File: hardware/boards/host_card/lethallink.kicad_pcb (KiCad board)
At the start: 6 copper layers, 121.2 x 98.4 mm, 218 parts, among them J1 PCIe-x4, J2 USB3_Micro_B_Amphenol, J3 Conn_02x05_Odd_Even, J4 Conn_02x04_Odd_Even, J5 Conn_02x04_Odd_Even, J6 SODIMM_260, Q1 Q_NMOS_GSD, Q2 Q_NMOS_GSD, Q3 Q_NMOS_GSD, Q4 Q_NMOS_GSD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

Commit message: Some more messing about with the DDR3 modules
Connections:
- U8 pad N2: Net-(U8-PadN2) -> /DDR3 Cache/A3
- U8 pad N3: Net-(U8-PadN3) -> /DDR3 Cache/A0
- U8 pad P2: Net-(U8-PadP2) -> /DDR3 Cache/A5
- U8 pad P3: Net-(U8-PadP3) -> /DDR3 Cache/A2
- U8 pad P7: Net-(U8-PadP7) -> /DDR3 Cache/A1
- U8 pad P8: Net-(U8-PadP8) -> /DDR3 Cache/A4
- U8 pad R2: Net-(U8-PadR2) -> /DDR3 Cache/A7
- U8 pad R3: Net-(U8-PadR3) -> /DDR3 Cache/A9
- U8 pad R8: Net-(U8-PadR8) -> /DDR3 Cache/A6
- U8 pad T8: Net-(U8-PadT8) -> /DDR3 Cache/A8

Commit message: Roughly grouped unplaced parts together based on what they are related to
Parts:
- added D12: RClamp0512, lethalbit:RClamp0512, F.Cu at (25.8, 57.5)
- moved D10 230.4 mm to (36.2, 167.0)
- moved C54 227.6 mm to (30.8, 167.1)
- moved R51 223.9 mm to (26.8, 166.9)
- moved R47 223.6 mm to (43.0, 162.4)
- moved R49 223.0 mm to (26.8, 162.9)
- moved R50 221.7 mm to (26.8, 158.2)
- moved D9 220.9 mm to (35.9, 162.9)
- moved Q6 219.6 mm to (36.1, 158.2)
- moved R48 218.7 mm to (31.0, 163.2)
- moved SW2 213.2 mm to (27.2, 150.4)
- moved C27 212.2 mm to (103.9, 175.2)
- moved D8 211.5 mm to (31.4, 158.1)
- moved C23 207.3 mm to (103.2, 173.4)
- moved C24 207.3 mm to (95.2, 169.4)
- moved C26 207.3 mm to (101.2, 175.4)
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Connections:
- net Net-(U4-PadB7) renamed /DDR3 Cache/DQSU0-
- net Net-(U4-PadC7) renamed /DDR3 Cache/DQSU0+
- net Net-(U4-PadD3) renamed /DDR3 Cache/DMU0
- net Net-(U4-PadE7) renamed /DDR3 Cache/DML0
- net Net-(U4-PadF3) renamed /DDR3 Cache/DQSL0+
- net Net-(U4-PadG3) renamed /DDR3 Cache/DQSL0-
- net Net-(U8-PadB7) renamed /DDR3 Cache/DQSU1-
- net Net-(U8-PadC7) renamed /DDR3 Cache/DQSU1+
- net Net-(U8-PadD3) renamed /DDR3 Cache/DMU1
- net Net-(U8-PadE7) renamed /DDR3 Cache/DML1
- net Net-(U8-PadF3) renamed /DDR3 Cache/DQSL1+
- net Net-(U8-PadG3) renamed /DDR3 Cache/DQSL1-
- U4 pad J3: Net-(U4-PadJ3) -> /DDR3 Cache/~RAS
- U4 pad J7: Net-(U4-PadJ7) -> /DDR3 Cache/CK+
- U4 pad K1: Net-(U4-PadK1) -> /DDR3 Cache/ODT
- U4 pad K3: Net-(U4-PadK3) -> /DDR3 Cache/~CAS
- U4 pad K7: Net-(U4-PadK7) -> /DDR3 Cache/CK-
- U4 pad K9: Net-(U4-PadK9) -> /DDR3 Cache/CKE
- U4 pad L2: Net-(U4-PadL2) -> /DDR3 Cache/~CS
- U4 pad L3: Net-(U4-PadL3) -> /DDR3 Cache/~WE
- U4 pad T2: Net-(U4-PadT2) -> /DDR3 Cache/~RESET
- U8 pad J3: Net-(U8-PadJ3) -> /DDR3 Cache/~RAS
- U8 pad J7: Net-(U8-PadJ7) -> /DDR3 Cache/CK+
- U8 pad K1: Net-(U8-PadK1) -> /DDR3 Cache/ODT
- U8 pad K3: Net-(U8-PadK3) -> /DDR3 Cache/~CAS
- U8 pad K7: Net-(U8-PadK7) -> /DDR3 Cache/CK-
- U8 pad K9: Net-(U8-PadK9) -> /DDR3 Cache/CKE
- U8 pad L2: Net-(U8-PadL2) -> /DDR3 Cache/~CS
- U8 pad L3: Net-(U8-PadL3) -> /DDR3 Cache/~WE
- U8 pad T2: Net-(U8-PadT2) -> /DDR3 Cache/~RESET
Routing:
- net GND: track 63.8 -> 64.1 mm, vias 72 -> 73

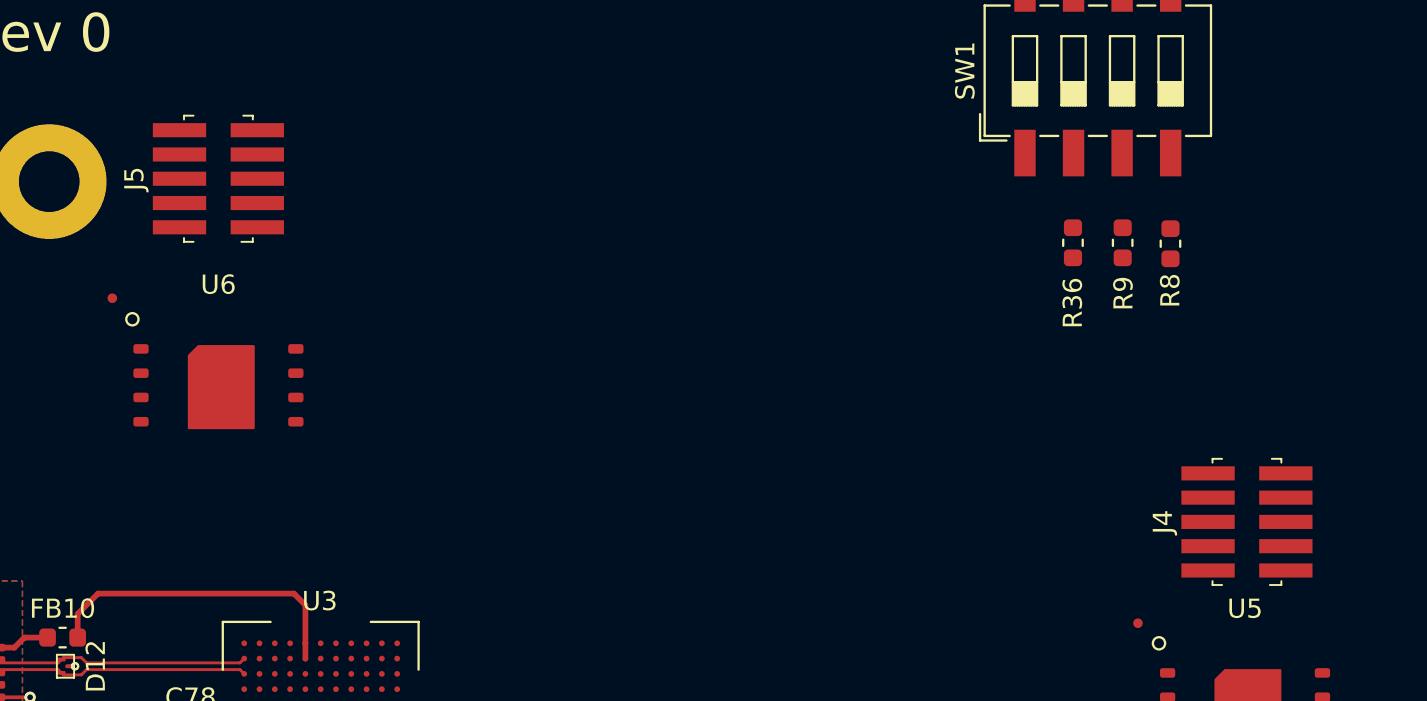
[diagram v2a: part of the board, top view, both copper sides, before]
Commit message: Added a pin-header for the FPGA SPI flash lines to allow for the USB PHY to do a DFU update of the gateware when closed
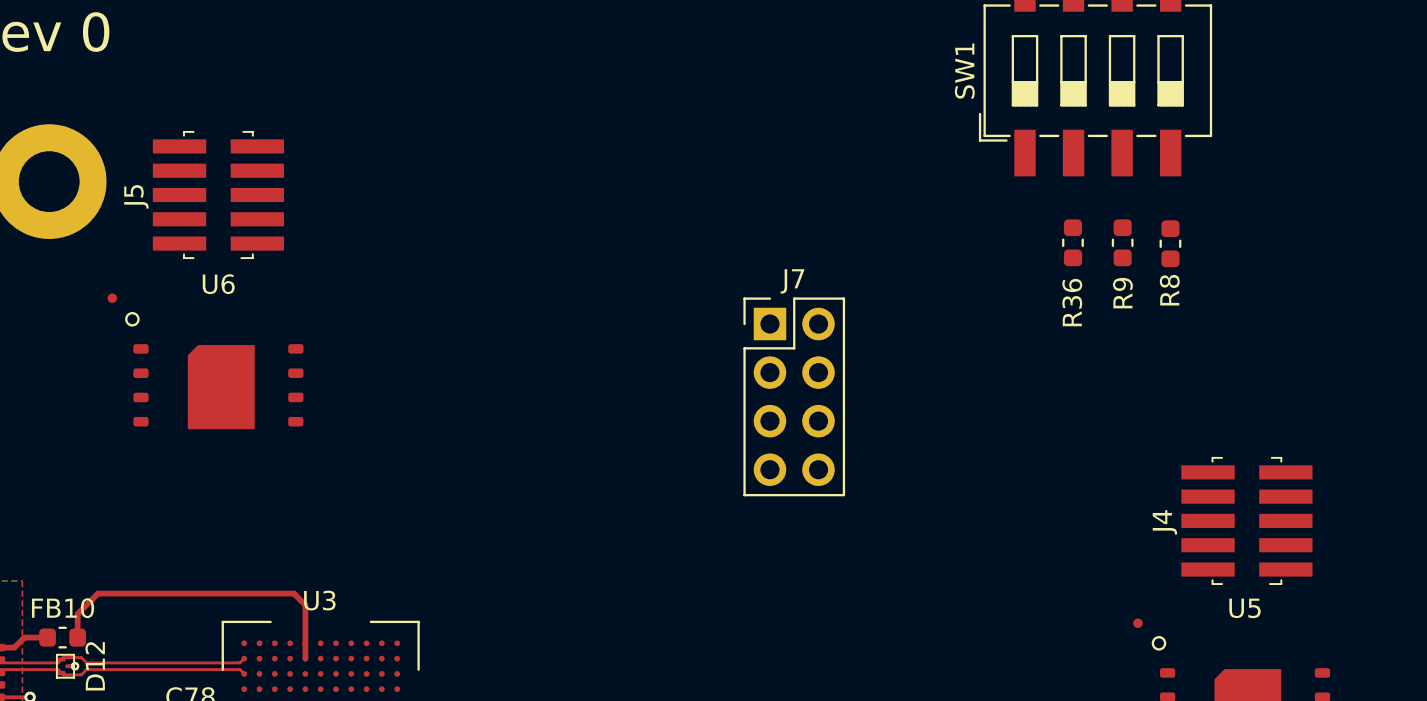
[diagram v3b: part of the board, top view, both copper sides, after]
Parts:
- added J7: Conn_02x04_Odd_Even, Connector_PinHeader_2.54mm:PinHeader_2x04_P2.54mm_Vertical, F.Cu at (62.6, 39.5)
- moved J5 0.85 mm to (33.8, 32.8)
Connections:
- J4 pad 1: /Boot Config/~RESET -> /Boot Config/~INIT
- J4 pad 2: /Boot Config/~INIT -> /Boot Config/~RESET
- J4 pad 3: +3V3 -> GND
- J4 pad 4: GND -> +3V3
- J5 pad 1: /Boot Config/~PHY_RESET -> GND
- J5 pad 2: GND -> /Boot Config/~PHY_RESET
- J5 pad 3: +3V3 -> GND
- J5 pad 4: GND -> +3V3
- J5 pad 5: Net-(J5-Pad5) -> /Boot Config/FPGA_DI
- J5 pad 7: Net-(J5-Pad7) -> /Boot Config/FPGA_CLK
- J5 pad 8: Net-(J5-Pad8) -> /Boot Config/FPGA_DO
- R42 pad 1: Net-(J4-Pad8) -> Net-(J4-Pad7)
- R43 pad 2: Net-(J4-Pad5) -> Net-(J4-Pad6)
- R44 pad 2: Net-(J4-Pad7) -> Net-(J4-Pad8)
- R45 pad 2: Net-(J4-Pad10) -> Net-(J4-Pad9)
- R46 pad 2: Net-(J4-Pad6) -> Net-(J4-Pad5)
- U1 pad R2: Net-(J4-Pad9) -> Net-(J4-Pad10)
- U1 pad V2: Net-(J4-Pad6) -> Net-(J4-Pad5)
- U1 pad W1: Net-(J4-Pad10) -> Net-(J4-Pad9)
- U1 pad W2: Net-(J4-Pad7) -> Net-(J4-Pad8)
- U1 pad Y2: Net-(J4-Pad5) -> Net-(J4-Pad6)
- U3 pad C1: Net-(J5-Pad9) -> Net-(J5-Pad10)
- U3 pad C2: Net-(J5-Pad7) -> /Boot Config/FPGA_DO
- U3 pad C4: Net-(U3-PadC4) -> /Boot Config/~FPGA_CS
- U3 pad D4: Net-(J5-Pad8) -> /Boot Config/FPGA_CLK
- U3 pad D5: Net-(J5-Pad6) -> /Boot Config/FPGA_DI
- U5 pad 1: Net-(J4-Pad9) -> Net-(J4-Pad10)
- U5 pad 2: Net-(J4-Pad7) -> Net-(J4-Pad8)
- U5 pad 3: Net-(J4-Pad5) -> Net-(J4-Pad6)
- U5 pad 5: Net-(J4-Pad6) -> Net-(J4-Pad5)
- U5 pad 6: Net-(J4-Pad8) -> Net-(J4-Pad7)
- U5 pad 7: Net-(J4-Pad10) -> Net-(J4-Pad9)
- U6 pad 1: Net-(J5-Pad9) -> Net-(J5-Pad10)
- U6 pad 2: Net-(J5-Pad7) -> /Boot Config/FPGA_DO
- U6 pad 3: Net-(J5-Pad5) -> Net-(J5-Pad6)
- U6 pad 5: Net-(J5-Pad6) -> /Boot Config/FPGA_DI
- U6 pad 6: Net-(J5-Pad8) -> /Boot Config/FPGA_CLK
- U6 pad 7: Net-(J5-Pad10) -> Net-(J5-Pad9)

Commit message: Hooked up the PCIe SMBUS and JTAG lines to the FPGA, might need to shuffle the signals around a little bit to get it to route nicely
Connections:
- U1 pad J4: Net-(U1-PadJ4) -> /AUX Control/PCIe_TMS
- U1 pad K4: Net-(U1-PadK4) -> /AUX Control/PCIe_TDO
- U1 pad L1: Net-(U1-PadL1) -> /AUX Control/PCIe_SMCLK
- U1 pad M1: Net-(U1-PadM1) -> /AUX Control/PCIe_SMDAT
- U1 pad M4: Net-(U1-PadM4) -> /AUX Control/PCIe_TCK
- U1 pad N4: Net-(U1-PadN4) -> /AUX Control/PCIe_TDI
- U1 pad P4: Net-(U1-PadP4) -> /AUX Control/PCIe_TRST#

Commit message: Added the remainder of the PCIe aux signals to the FPGA
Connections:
- U1 pad P1: Net-(U1-PadP1) -> /AUX Control/CLKREQ#
- U1 pad P2: Net-(U1-PadP2) -> /AUX Control/WAKE#
- U1 pad P3: Net-(U1-PadP3) -> /AUX Control/PERST#

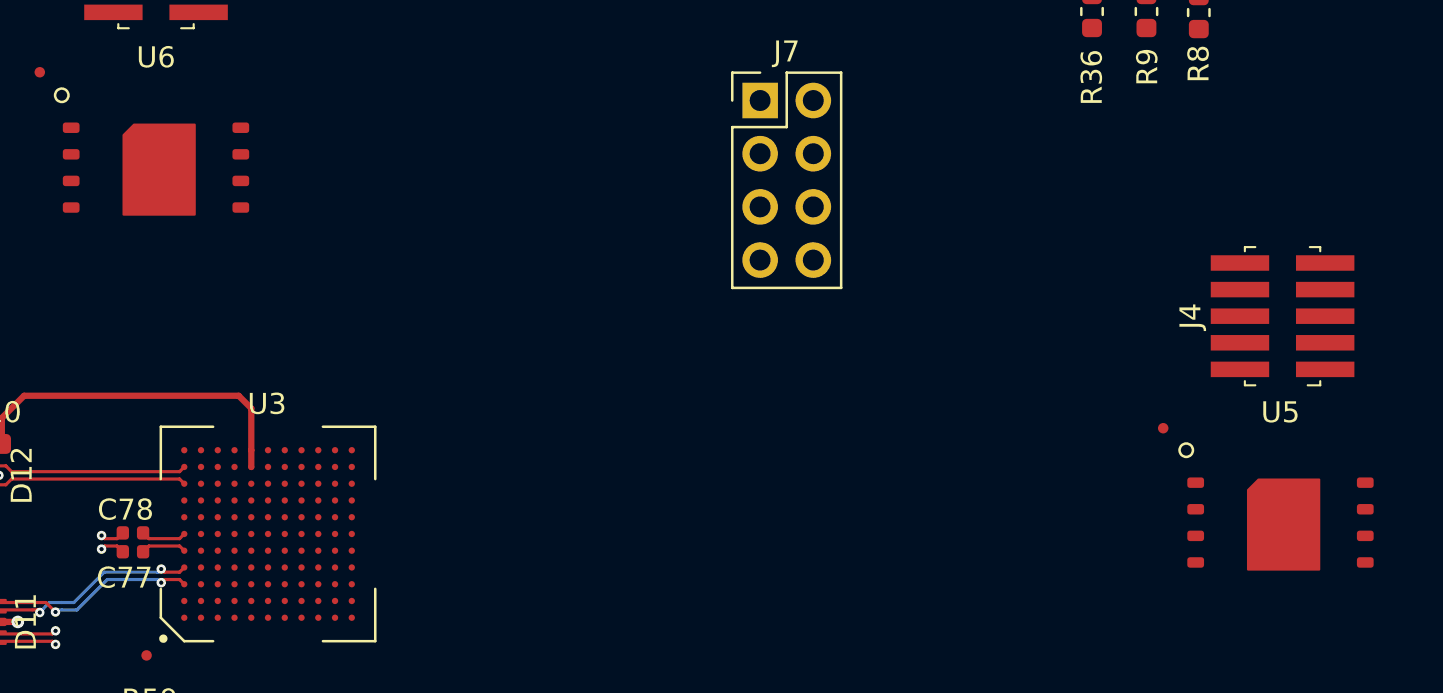
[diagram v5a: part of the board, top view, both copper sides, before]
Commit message: Updated the SPI flash footprints to have the exposed pad joined to the gnd properly
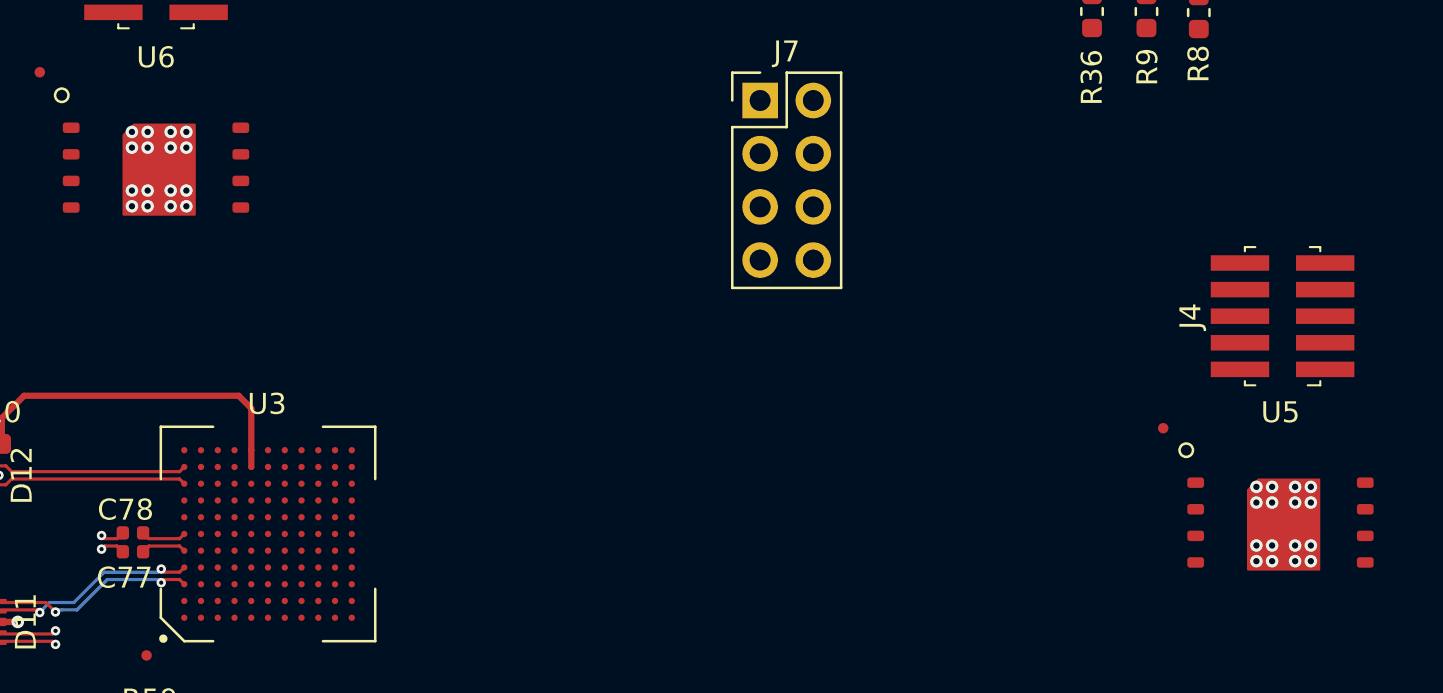
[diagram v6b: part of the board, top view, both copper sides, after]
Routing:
- net GND: vias 73 -> 105

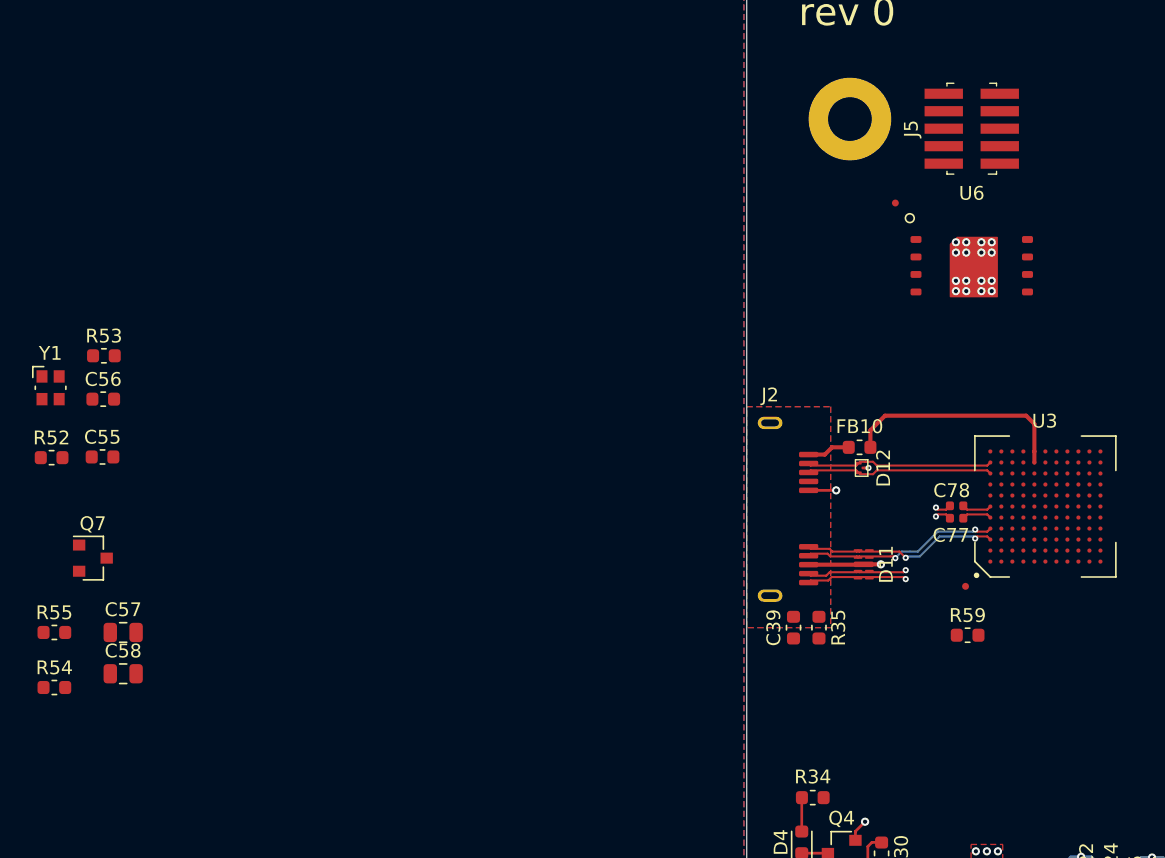
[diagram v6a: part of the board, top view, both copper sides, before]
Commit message: Started poking the SPI flash for the USB PHY
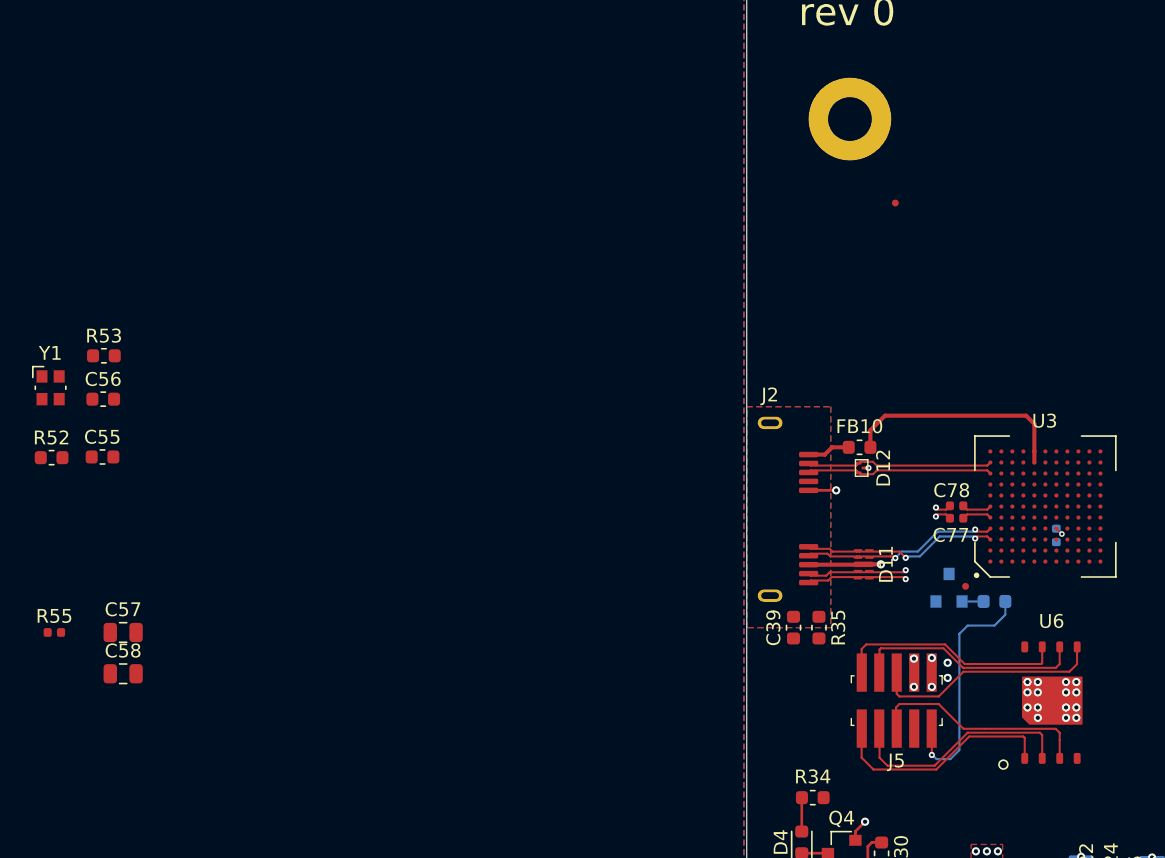
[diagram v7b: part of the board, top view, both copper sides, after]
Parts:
- Q7, R54: moved to B.Cu
- R55: footprint Resistor_SMD:R_0603_1608Metric -> Resistor_SMD:R_0402_1005Metric
- R59: footprint Resistor_SMD:R_0603_1608Metric -> Resistor_SMD:R_0402_1005Metric; moved to B.Cu
- moved R54 68.6 mm to (35.5, 67.2), turned to 180 degrees
- moved Q7 62.2 mm to (32.1, 66.2), turned to 90 degrees
- moved J5 41.9 mm to (28.4, 74.3), turned to 180 degrees
- moved U6 32.2 mm to (39.6, 74.5), turned to 90 degrees
- moved R59 9.70 mm to (40.0, 62.4), turned to 90 degrees
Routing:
- net /Boot Config/~PHY_RESET: track 0.00 -> 17.7 mm, vias 0 -> 1
- net /Boot Config/FPGA_DO: track 0.00 -> 16.9 mm
- net /Boot Config/FPGA_DI: track 0.00 -> 16.9 mm
- net /Boot Config/FPGA_CLK: track 0.00 -> 16.8 mm
- net Net-(J5-Pad9): track 0.00 -> 16.8 mm
- net Net-(J5-Pad10): track 0.00 -> 16.8 mm
- net Net-(J5-Pad6): track 0.00 -> 16.3 mm
- net Net-(Q7-Pad1): track 0.00 -> 1.50 mm
- net /USB3 Interface/PMODE_0: track 0.00 -> 1.13 mm, vias 0 -> 1
- net GND: vias 105 -> 110

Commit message: Some updates with the DDR3, gonna need to re-assign most of the pins to make routing it not a massive pain in the ass
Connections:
- U1 pad C20: /DDR3 Cache/A0 -> /DDR3 Cache/BA1
- U1 pad D19: /DDR3 Cache/A1 -> /DDR3 Cache/BA2
- U1 pad D20: /DDR3 Cache/A2 -> /DDR3 Cache/~RAS
- U1 pad E19: /DDR3 Cache/A3 -> /DDR3 Cache/~CAS
- U1 pad E20: /DDR3 Cache/A4 -> /DDR3 Cache/~WE
- U1 pad F17: Net-(U1-PadF17) -> /DDR3 Cache/A14
- U1 pad F18: Net-(U1-PadF18) -> /DDR3 Cache/A15
- U1 pad F19: /DDR3 Cache/A5 -> /DDR3 Cache/CKE0
- U1 pad F20: /DDR3 Cache/A6 -> /DDR3 Cache/A5
- U1 pad G16: Net-(U1-PadG16) -> /DDR3 Cache/A12
- U1 pad G18: Net-(U1-PadG18) -> /DDR3 Cache/A13
- U1 pad G19: /DDR3 Cache/A8 -> Net-(U1-PadG19)
- U1 pad G20: /DDR3 Cache/A7 -> /DDR3 Cache/CKE1
- U1 pad H16: Net-(U1-PadH16) -> /DDR3 Cache/A11
- U1 pad H17: Net-(U1-PadH17) -> /DDR3 Cache/A9
- U1 pad H18: Net-(U1-PadH18) -> /DDR3 Cache/A10
- U1 pad H20: /DDR3 Cache/A9 -> Net-(U1-PadH20)
- U1 pad J16: /DDR3 Cache/A15 -> /DDR3 Cache/A7
- U1 pad J17: /DDR3 Cache/A14 -> /DDR3 Cache/A8
- U1 pad J18: /DDR3 Cache/A10 -> /DDR3 Cache/ODT0
- U1 pad J19: /DDR3 Cache/A12 -> /DDR3 Cache/A3
- U1 pad J20: /DDR3 Cache/CLK+ -> /DDR3 Cache/A1
- U1 pad K18: /DDR3 Cache/A11 -> /DDR3 Cache/A4
- U1 pad K19: /DDR3 Cache/A13 -> /DDR3 Cache/A2
- U1 pad K20: /DDR3 Cache/CLK- -> /DDR3 Cache/A0
- U1 pad L16: Net-(U1-PadL16) -> /DDR3 Cache/DQL1
- U1 pad L18: Net-(U1-PadL18) -> /DDR3 Cache/DQL2
- U1 pad L20: Net-(U1-PadL20) -> /DDR3 Cache/CLK+
- U1 pad M17: /DDR3 Cache/BA2 -> /DDR3 Cache/DQSL0-
- U1 pad M18: Net-(U1-PadM18) -> /DDR3 Cache/DQL3
- U1 pad M19: Net-(U1-PadM19) -> /DDR3 Cache/DQL0
- U1 pad M20: Net-(U1-PadM20) -> /DDR3 Cache/CLK-
- U1 pad N16: /DDR3 Cache/BA1 -> /DDR3 Cache/DQSL0+
- U1 pad N17: /DDR3 Cache/BA0 -> /DDR3 Cache/DQL5
- U1 pad N18: Net-(U1-PadN18) -> /DDR3 Cache/DQL4
- U1 pad N19: Net-(U1-PadN19) -> /DDR3 Cache/~CS0
- U1 pad N20: Net-(U1-PadN20) -> /DDR3 Cache/~CS1
- U1 pad P18: Net-(U1-PadP18) -> /DDR3 Cache/DQU1
- U1 pad P19: Net-(U1-PadP19) -> /DDR3 Cache/DQU0
- U1 pad P20: Net-(U1-PadP20) -> /DDR3 Cache/DQU2
- U1 pad R16: Net-(U1-PadR16) -> /DDR3 Cache/DQL7
- U1 pad R17: Net-(U1-PadR17) -> /DDR3 Cache/DQL6
- U1 pad R18: Net-(U1-PadR18) -> /DDR3 Cache/DQSU0-
- U1 pad R20: Net-(U1-PadR20) -> /DDR3 Cache/DQU3
- U1 pad T16: Net-(U1-PadT16) -> /DDR3 Cache/ODT1
- U1 pad T19: Net-(U1-PadT19) -> /DDR3 Cache/DQSU0+
- U1 pad U17: Net-(U1-PadU17) -> /DDR3 Cache/DQU7
- U1 pad U18: Net-(U1-PadU18) -> /DDR3 Cache/DQU6
- U1 pad U19: Net-(U1-PadU19) -> /DDR3 Cache/DQU5
- U1 pad U20: Net-(U1-PadU20) -> /DDR3 Cache/DQU4
- U4 pad K1: /DDR3 Cache/ODT -> /DDR3 Cache/ODT0
- U4 pad K9: /DDR3 Cache/CKE -> /DDR3 Cache/CKE0
- U4 pad L2: /DDR3 Cache/~CS -> /DDR3 Cache/~CS0
- U8 pad B7: /DDR3 Cache/DQSU1- -> /DDR3 Cache/DQSU0-
- U8 pad C7: /DDR3 Cache/DQSU1+ -> /DDR3 Cache/DQSU0+
- U8 pad D3: /DDR3 Cache/DMU1 -> /DDR3 Cache/DMU0
- U8 pad E7: /DDR3 Cache/DML1 -> /DDR3 Cache/DML0
- U8 pad F3: /DDR3 Cache/DQSL1+ -> /DDR3 Cache/DQSL0+
- U8 pad G3: /DDR3 Cache/DQSL1- -> /DDR3 Cache/DQSL0-
- U8 pad K1: /DDR3 Cache/ODT -> /DDR3 Cache/ODT1
- U8 pad K9: /DDR3 Cache/CKE -> /DDR3 Cache/CKE1
- U8 pad L2: /DDR3 Cache/~CS -> /DDR3 Cache/~CS1
